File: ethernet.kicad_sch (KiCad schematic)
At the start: 2 parts, among them J1 SI-52008-F, U2 LAN8742A

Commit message: Worked on ETH
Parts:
- added C2: C_Small, symbol Device:C_Small
- added D10, D3, D4, D5, D6, D7, D8, D9: D_Schottky, symbol Device:D_45deg
- added D11: D_Schottky, Diode_SMD:D_SMA, symbol Device:D_Schottky
- added MD1: MURATA_MYBSP00502ABF, MURATA_MYBSP00502ABF:MURATA_MYBSP00502ABF_0, symbol MURATA_MYBSP00502ABF:MURATA_MYBSP00502ABF
- added R10, R4, R5, R6, R9: 270R, symbol Device:R
- added R11: 33R, symbol Device:R
- added R7: 12.1kR 1%, symbol Device:R
- added R8: 4.7kR, symbol Device:R
- added Y1: ECS-3225MVLC-500-CN-TR, Oscillator:Oscillator_SMD_ECS_2520MV-xxx-xx-4Pin_2.5x2.0mm, symbol Oscillator:ECS-2520MV-xxx-xx
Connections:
- net at U2.10 (RXER/PHYAD0): now also R10.1
- net ETH_CRS_DV: now reaches U2.11 (CRS_DV/MODE2)
- net ETH_MDIO: now reaches U2.12 (MDIO)
- net ETH_MDC: now reaches U2.13 (MDC)
- net ETH_nINT: now reaches U2.14 (~{INT}/REFCLKO)
- net ETH_nINT: now also R9.1
- net ETH_nRST: now reaches U2.15 (~{RST})
- net ETH_nRST: now also R6.1
- net ETH_TXEN: now reaches U2.16 (TXEN)
- net ETH_TXD0: now reaches U2.17 (TXD0)
- net ETH_TXD1: now reaches U2.18 (TXD1)
- net at U2.2 (LED2/~{INTSEL}): now also R4.1, R8.1
- net at U2.20 (TXN): now also J1.3 (TD-)
- net at U2.21 (TXP): now also J1.1 (TD+)
- net at U2.22 (RXN): now also J1.5 (RD-)
- net at U2.23 (RXP): now also J1.4 (RD+)
- net at U2.24 (RBIAS): now also R7.2
- net GND: now reaches U2.25 (VSS)
- net GND: now also J1.G_K, C2.2, MD1.3 (-VOUT), R7.1, Y1.2 (GND)
- net at U2.3 (LED1/REGOFF): now also R5.1
- net ETH_REF_CLK: now reaches U2.5 (XTAL1/CLKIN)
- net ETH_REF_CLK: now also R11.2
- net ETH_RXD1: now reaches U2.7 (RXD1/MODE1)
- net ETH_RXD0: now reaches U2.8 (RXD0/MODE0)
- net at J1.10 (VC+_P10): now also D6.1 (K), D8.2 (A)
- net at J1.11 (VC-_P11): now also D10.2 (A), D9.1 (K)
- net at J1.8 (VC+_P8): now also D4.1 (K), D7.2 (A)
- net at J1.9 (VC-_P9): now also D3.2 (A), D5.1 (K)
- net at J1.G_A: now also R5.2
- net +3V3: now reaches J1.Y_A
- net +3V3: now also C2.1, R10.2, R6.2, R8.2, R9.2, Y1.4 (VDD)
- net at J1.Y_K: now also R4.2
- new net: D4.2 (A), D5.2 (A), D6.2 (A), D9.2 (A), MD1.2 (-VIN)
- new net: R11.1, Y1.3 (OUT)
- new net: D10.1 (K), D3.1 (K), D7.1 (K), D8.1 (K), MD1.1 (+VIN)
- new net: D11.2 (A), MD1.4 (+VOUT)
- new net +5V: D11.1 (K)
- no-connect marks 0 -> 2
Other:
- moved on the sheet: J1, U2

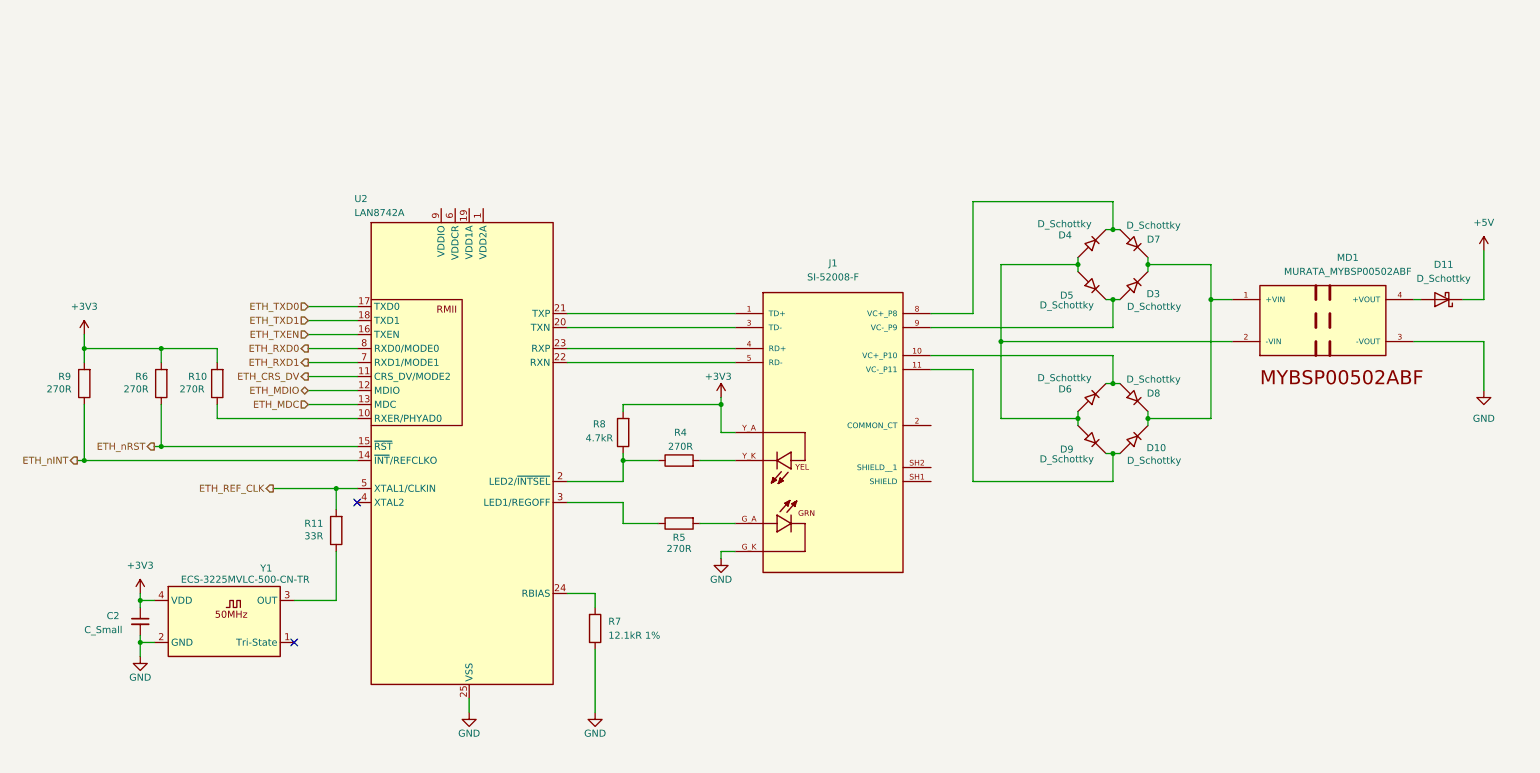
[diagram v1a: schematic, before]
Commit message: Added SDMMC
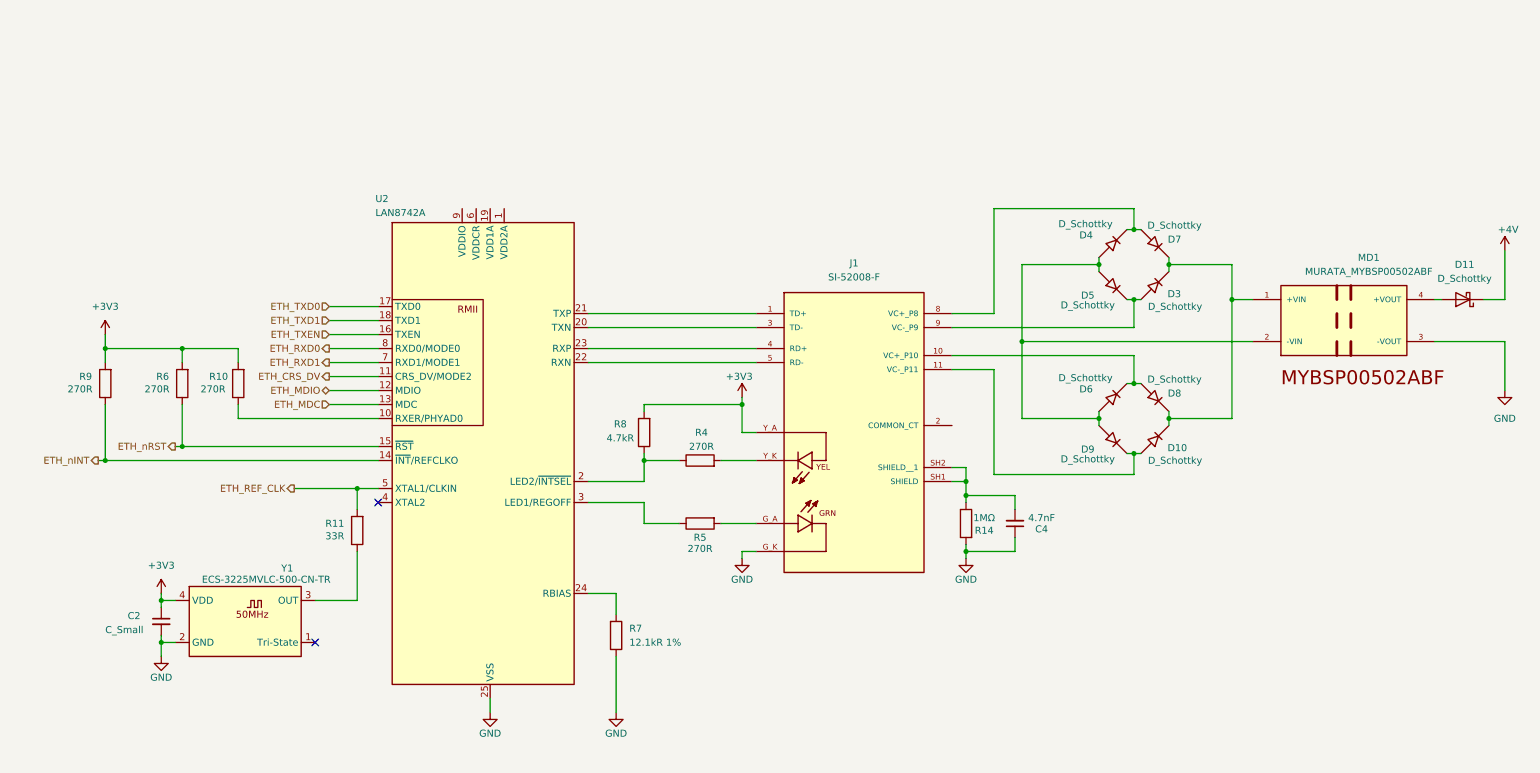
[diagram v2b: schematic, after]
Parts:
- added C4: 4.7nF, Capacitor_SMD:C_0805_2012Metric_Pad1.18x1.45mm_HandSolder, symbol Device:C_Small
- added R14: 1MΩ, Resistor_SMD:R_0805_2012Metric_Pad1.20x1.40mm_HandSolder, symbol Device:R
- C2: footprint (none) -> Capacitor_SMD:C_0805_2012Metric_Pad1.18x1.45mm_HandSolder
- D10, D3, D4, D5, D6, D7, D8, D9: footprint (none) -> Diode_SMD:Nexperia_CFP3_SOD-123W
- D11: footprint Diode_SMD:D_SMA -> Diode_SMD:Nexperia_CFP3_SOD-123W
- MD1: footprint MURATA_MYBSP00502ABF:MURATA_MYBSP00502ABF_0 -> MYBSP00502ABF:MURATA_MYBSP00502ABF_0
- R10, R11, R4, R5, R6, R7, R8, R9: footprint (none) -> Resistor_SMD:R_0805_2012Metric_Pad1.20x1.40mm_HandSolder
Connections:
- net GND: now also C4.1, R14.2
- net at J1.SH1 (SHIELD): now also J1.SH2 (SHIELD__1), C4.2, R14.1
- net +5V renamed +4V
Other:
- moved on the sheet: C2, D10, D11, D3, D4, D5, D6, D7, D8, D9, J1, MD1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

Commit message: Worked on ETH PHY schematic
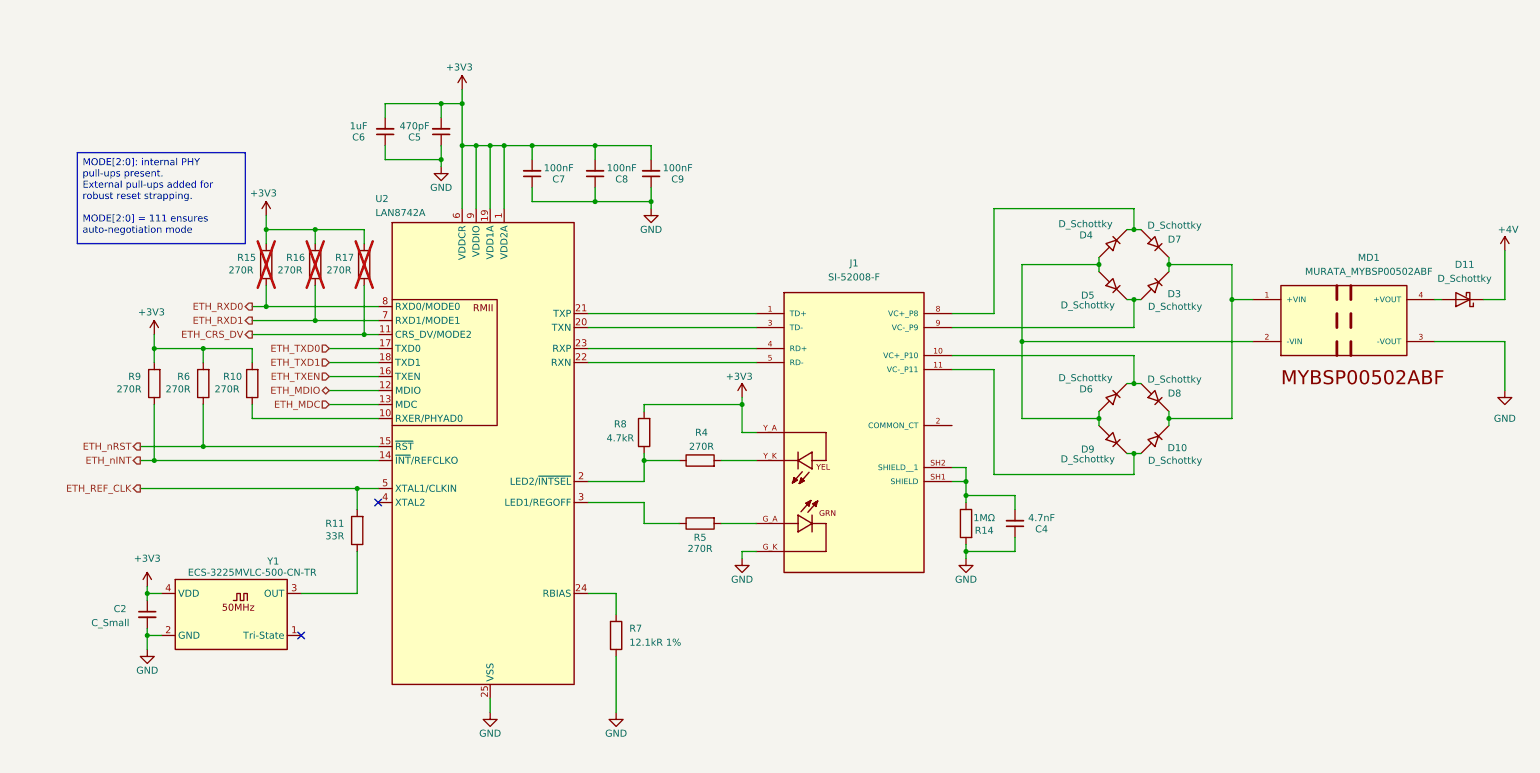
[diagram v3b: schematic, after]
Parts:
- added C5: 470pF, Capacitor_SMD:C_0805_2012Metric_Pad1.18x1.45mm_HandSolder, symbol Device:C_Small
- added C6: 1uF, Capacitor_SMD:C_0805_2012Metric_Pad1.18x1.45mm_HandSolder, symbol Device:C_Small
- added C7, C8, C9: 100nF, Capacitor_SMD:C_0805_2012Metric_Pad1.18x1.45mm_HandSolder, symbol Device:C_Small
- added R15, R16, R17: 270R, Resistor_SMD:R_0805_2012Metric_Pad1.20x1.40mm_HandSolder, symbol Device:R
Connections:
- net +3V3: now also U2.1 (VDD2A), U2.19 (VDD1A), U2.6 (VDDCR), U2.9 (VDDIO), C5.2, C6.2, C7.2, C8.2, C9.2, R15.2, R16.2, R17.2
- net ETH_CRS_DV: now also R17.1
- net ETH_RXD0: now also R15.1
- net ETH_RXD1: now also R16.1
- net GND: now also C5.1, C6.1, C7.1, C8.1, C9.1
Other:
- moved on the sheet: C2, R10, R6, R9, Y1

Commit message: improved ETH schematics
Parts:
- added C10, C11, C12, C13: 10pF, Capacitor_SMD:C_0805_2012Metric_Pad1.18x1.45mm_HandSolder, symbol Device:C_Small
- added C14: 22uF, Capacitor_SMD:C_0805_2012Metric_Pad1.18x1.45mm_HandSolder, symbol Device:C_Small
- added C15: 330uF, Capacitor_SMD:C_0805_2012Metric_Pad1.18x1.45mm_HandSolder, symbol Device:C_Small
- added L1: L, symbol Device:L
- added R18, R19, R20, R21: 49.9R, Resistor_SMD:R_0805_2012Metric_Pad1.20x1.40mm_HandSolder, symbol Device:R
- added R22, R23, R24: 33R, Resistor_SMD:R_0805_2012Metric_Pad1.20x1.40mm_HandSolder, symbol Device:R
- added R25: 10kR, Resistor_SMD:R_0805_2012Metric_Pad1.20x1.40mm_HandSolder, symbol Device:R
- R10: value 270R -> 1.5kR
- R15, R16, R17, R6, R9: value 270R -> 10kR
- R7: value 12.1kR 1% -> 12.1kR
- R8: value 4.7kR -> 10kR; now not fitted
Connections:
- net +3V3: now also L1.1; no longer C5.2, C6.2, C7.2, C8.2, U2.1 (VDD2A), U2.19 (VDD1A), U2.6 (VDDCR)
- net ETH_MDIO: now also R10.1
- net ETH_RXD0: now also R22.2; no longer R15.1, U2.8 (RXD0/MODE0)
- net ETH_RXD1: now also R23.2; no longer R16.1, U2.7 (RXD1/MODE1)
- net ETH_nINT: now also R6.1; no longer R9.1
- net ETH_nRST: now also R9.1; no longer R6.1
- net GND: now also C6.2, C10.1, C11.1, C12.1, C13.1, C14.1, C15.1, R25.1; no longer C6.1
- net at U2.10 (RXER/PHYAD0): now also R24.1; no longer R10.1
- net at J1.3 (TD-), U2.20 (TXN): now also C11.2, R20.1
- net at J1.1 (TD+), U2.21 (TXP): now also C10.2, R21.1
- net at J1.5 (RD-), U2.22 (RXN): now also C13.2, R18.1
- net at J1.4 (RD+), U2.23 (RXP): now also C12.2, R19.1
- net at R5.1, U2.3 (LED1/REGOFF): now also R25.2
- net VDDA: now reaches J1.2 (COMMON_CT)
- net VDDA: now also C7.2, C8.2, U2.1 (VDD2A), U2.19 (VDD1A), L1.2, R18.2, R19.2, R20.2, R21.2
- net at D11.2 (A), MD1.4 (+VOUT): now also C14.2, C15.2
- new net: C5.2, C6.1, U2.6 (VDDCR)
- new net: R16.1, R23.1, U2.7 (RXD1/MODE1)
- new net: R15.1, R22.1, U2.8 (RXD0/MODE0)
- new net ETH_RXER: R24.2
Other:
- note added: "1%"
- moved on the sheet: C2, C4, C5, C6, C7, C8, C9, D10, D11, D3, D4, D5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
